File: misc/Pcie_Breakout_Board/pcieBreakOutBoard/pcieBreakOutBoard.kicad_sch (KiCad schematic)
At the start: 1 part, among them J1 2041119-1 (Mini Pcie Express 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

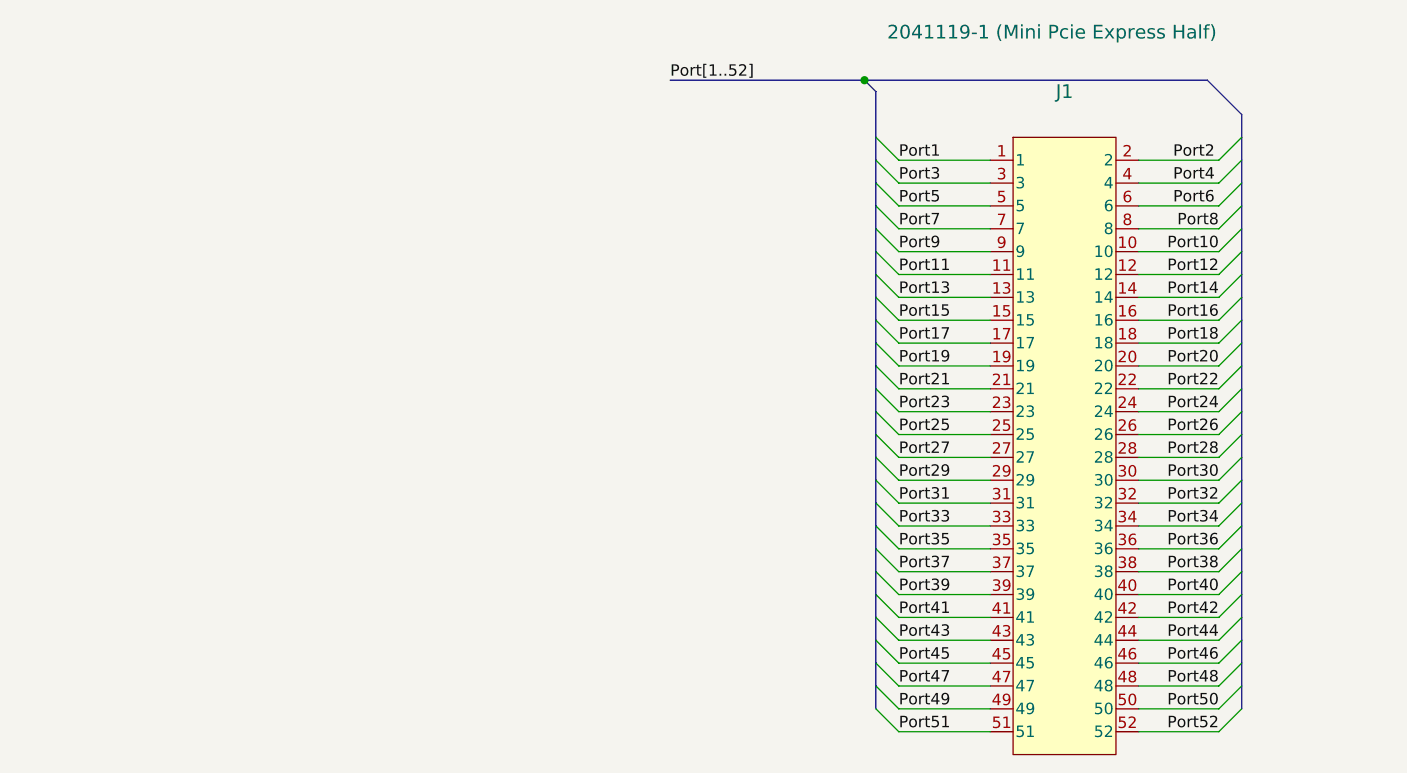
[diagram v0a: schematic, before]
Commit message: jtag
Added jtag and serial capabilities for the pcie breakout board
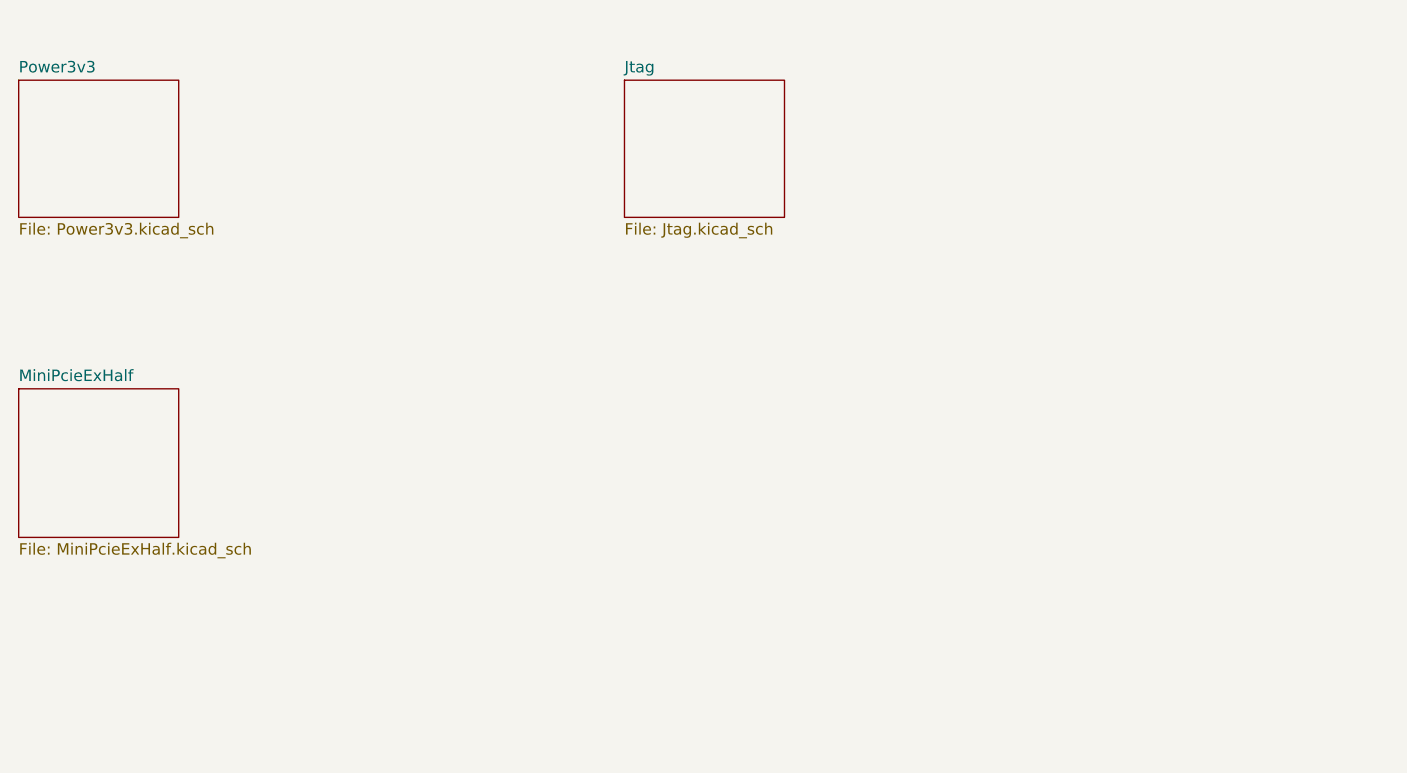
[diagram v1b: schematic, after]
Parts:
- removed J1: 2041119-1 (Mini Pcie Express Half), User_Footprint:CONN_2041119-1_TEC, symbol _Connectors:2041119-1
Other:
- added sheet Jtag (Jtag.kicad_sch)
- added sheet MiniPcieExHalf (MiniPcieExHalf.kicad_sch)
- added sheet Power3v3 (Power3v3.kicad_sch)

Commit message: Jtag
Added jtag and serial interface to the breakout board
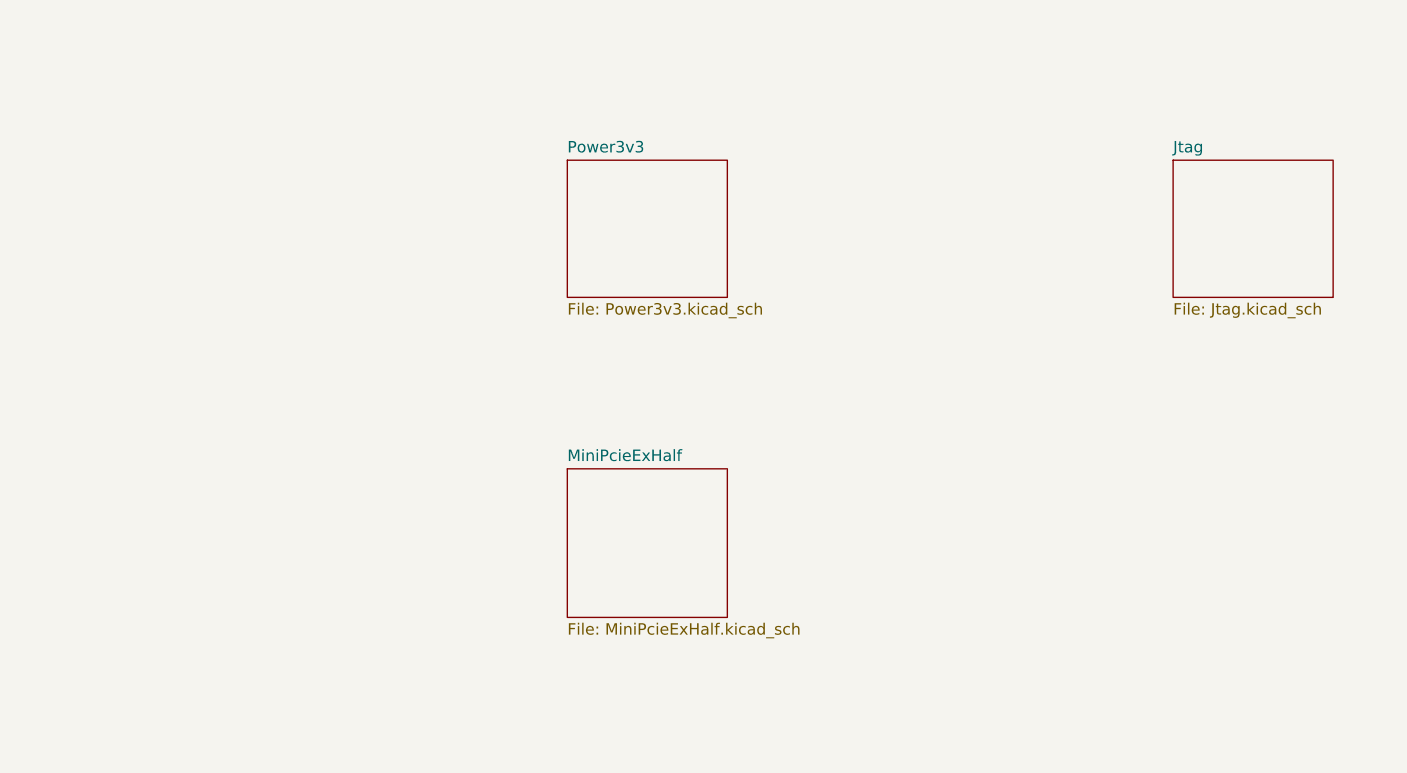
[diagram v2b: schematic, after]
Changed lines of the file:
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@@
 	(paper "A4")
 	(sheet
-		(at 40.64 87.63)
+		(at 101.6 96.52)
 		(size 17.78 16.51)
 		(exclude_from_sim no)
@@
 		)
 		(property "Sheetname" "MiniPcieExHalf"
-			(at 40.64 86.9184 0)
+			(at 101.6 95.8084 0)
 			(effects
 				(font
@@
 		)
 		(property "Sheetfile" "MiniPcieExHalf.kicad_sch"
-			(at 40.64 104.7246 0)
+			(at 101.6 113.6146 0)
 			(effects
 				(font
@@
 	)
 	(sheet
-		(at 107.95 53.34)
+		(at 168.91 62.23)
 		(size 17.78 15.24)
 		(exclude_from_sim no)
@@
 		)
 		(property "Sheetname" "Jtag"
-			(at 107.95 52.6284 0)
+			(at 168.91 61.5184 0)
 			(effects
 				(font
@@
 		)
 		(property "Sheetfile" "Jtag.kicad_sch"
-			(at 107.95 69.1646 0)
+			(at 168.91 78.0546 0)
 			(effects
 				(font
@@
 	)
 	(sheet
-		(at 40.64 53.34)
+		(at 101.6 62.23)
 		(size 17.78 15.24)
 		(exclude_from_sim no)
@@
 		)
 		(property "Sheetname" "Power3v3"
-			(at 40.64 52.6284 0)
+			(at 101.6 61.5184 0)
 			(effects
 				(font
@@
 		)
 		(property "Sheetfile" "Power3v3.kicad_sch"
-			(at 40.64 69.1646 0)
+			(at 101.6 78.0546 0)
 			(effects
 				(font

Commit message: layout
finished 70% of layout
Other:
- sheet Power3v3 renamed Power
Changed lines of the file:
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@@
 			(color 0 0 0 0.0000)
 		)
-		(property "Sheetname" "Power3v3"
+		(property "Sheetname" "Power"
 			(at 101.6 61.5184 0)
 			(effects
